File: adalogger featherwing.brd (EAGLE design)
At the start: 50.8 x 22.9 mm, 22 parts, among them IC1 RTC_PCF8523T, SW1 KMR2, X4 microsd, Y1 32khz

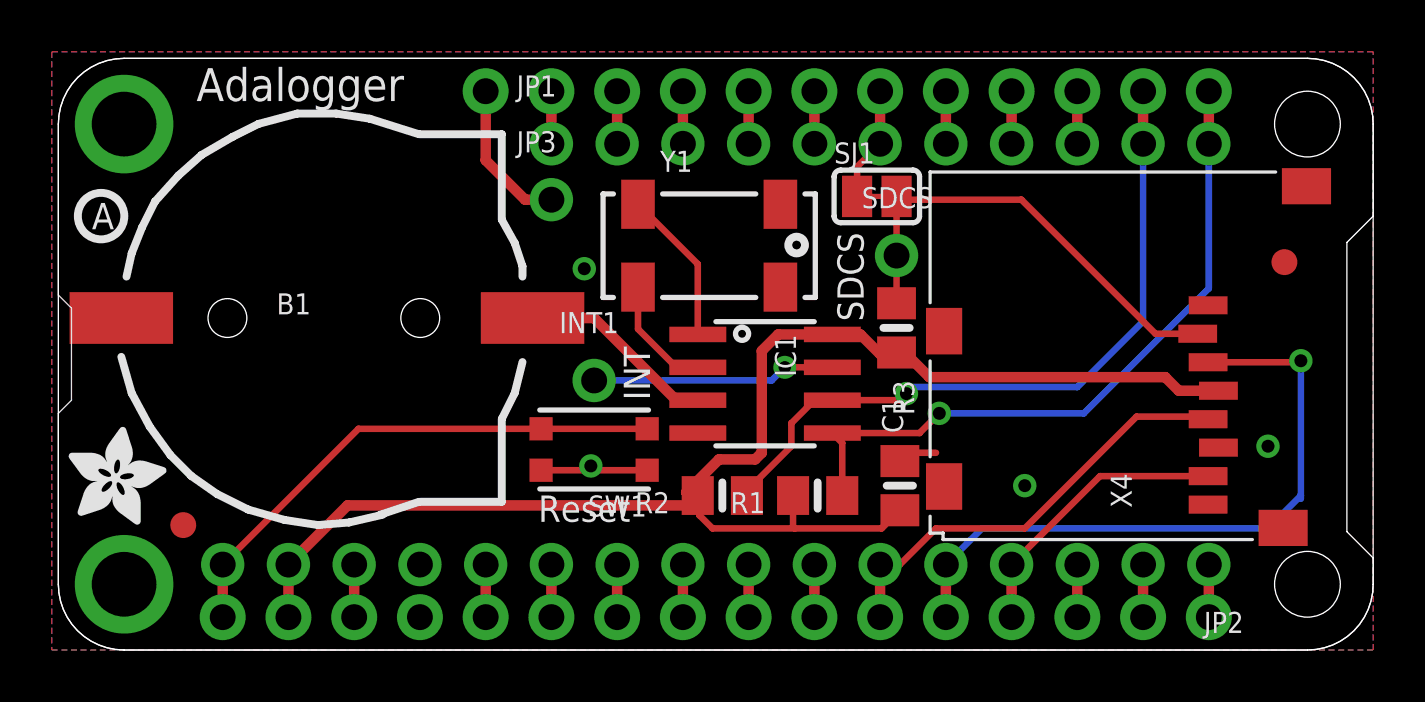
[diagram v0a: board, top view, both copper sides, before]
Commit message: added RC network on PCF vdd line
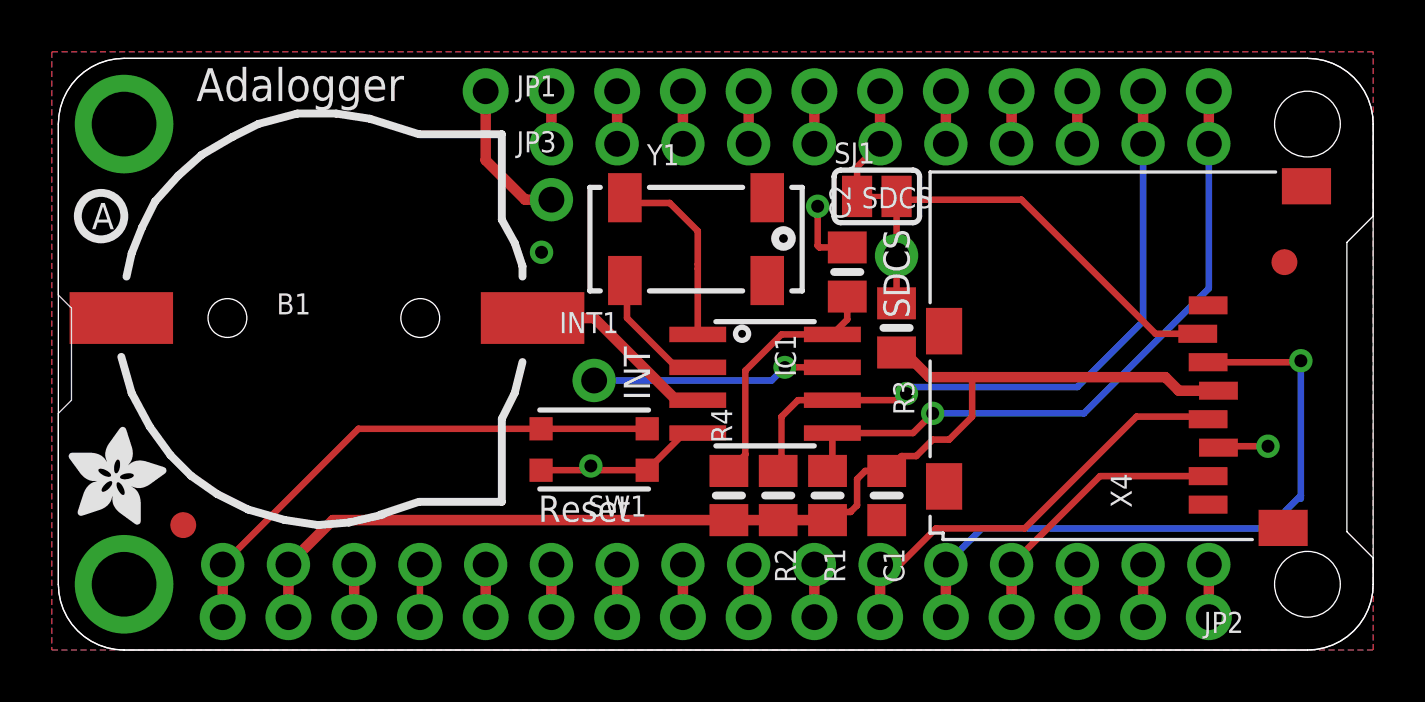
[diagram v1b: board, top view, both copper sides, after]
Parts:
- added C2: 10uF, microbuilder:0805-NO
- added R4: 1K, microbuilder:0805-NO
- moved R2 2.16 mm to (27.8, 5.97), turned to 270 degrees
- moved C1 0.64 mm to (32.0, 5.97), turned to 270 degrees
- moved Y1 0.57 mm to (24.6, 15.9)
- moved R1 0.38 mm to (29.7, 5.97), turned to 270 degrees
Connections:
- new net PCFVDD: C2.1, IC1.8, R4.2
- net +3V3: now also R4.1; no longer IC1.8
- net GND: now also C2.2
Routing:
- net +3V3: track 56.4 -> 46.0 mm
- net PCFVDD: track 0.00 -> 9.78 mm
- net GND: track 5.63 -> 13.4 mm
- net N$7: track 5.99 -> 7.35 mm
- net SCL: track 29.6 -> 28.6 mm
- net SDA: track 29.1 -> 28.1 mm
